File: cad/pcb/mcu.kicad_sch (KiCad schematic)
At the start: 22 parts, among them SW1 nRST, U1 nRF52810-QFxx, X1 SWD_Conn, Y1 32Meg, Y2 32.768k

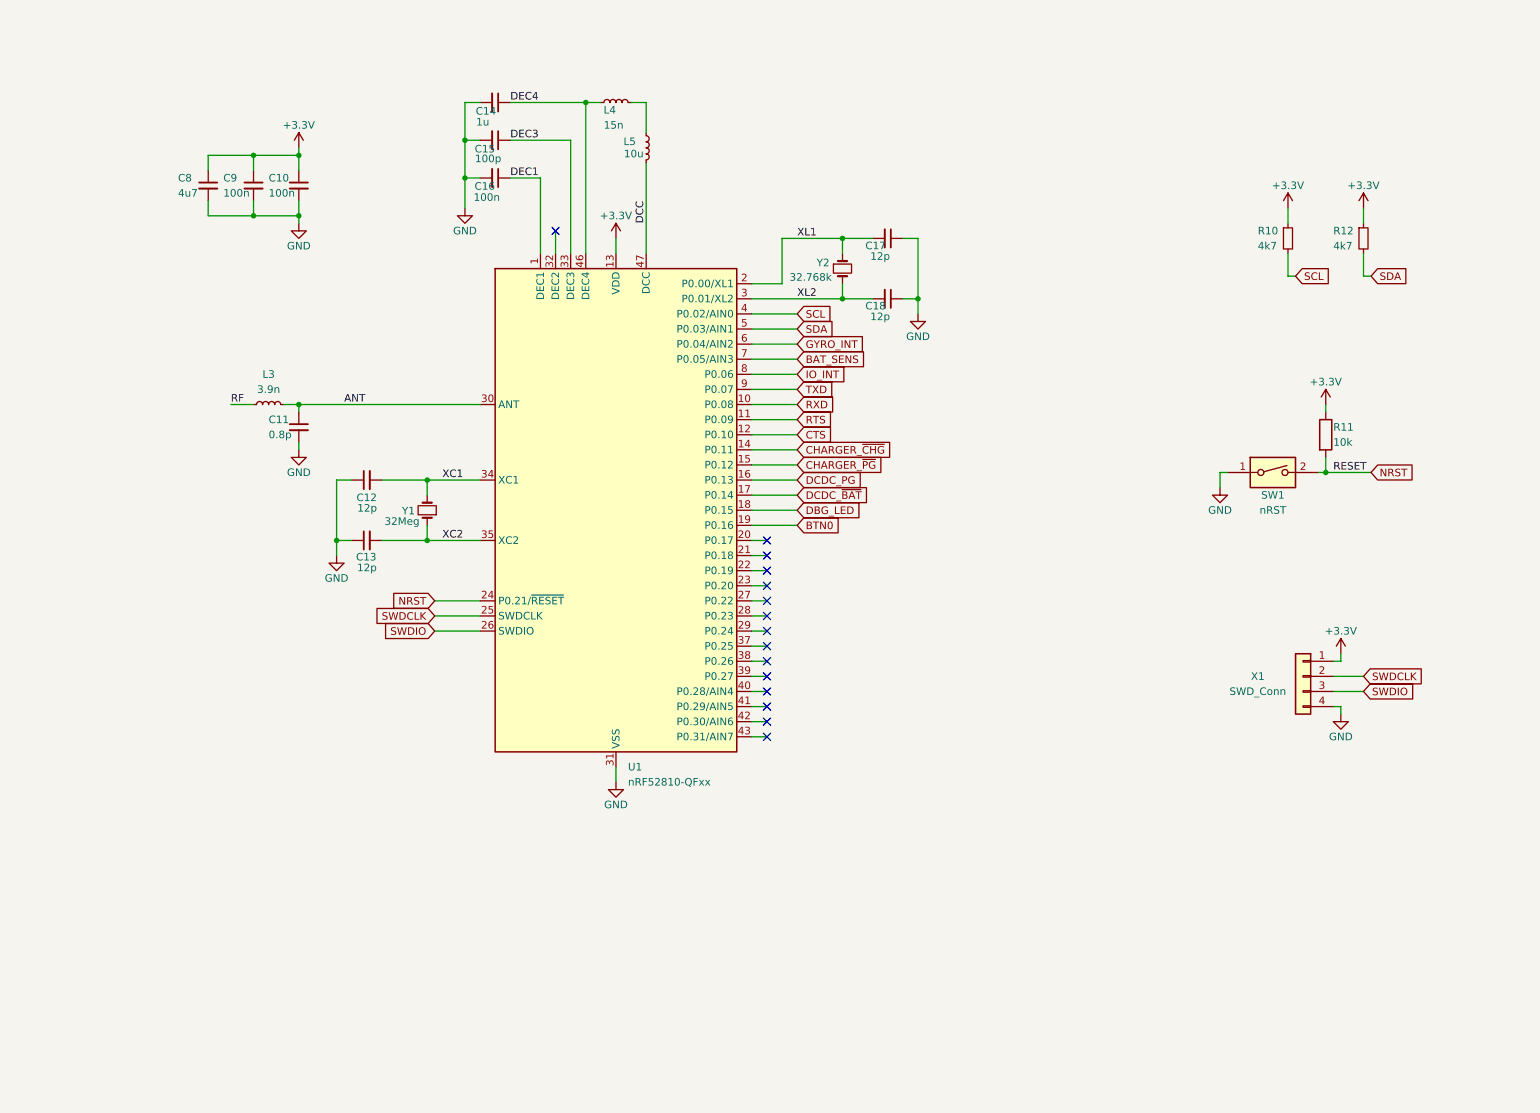
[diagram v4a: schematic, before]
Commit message: add LEDs for LED ring
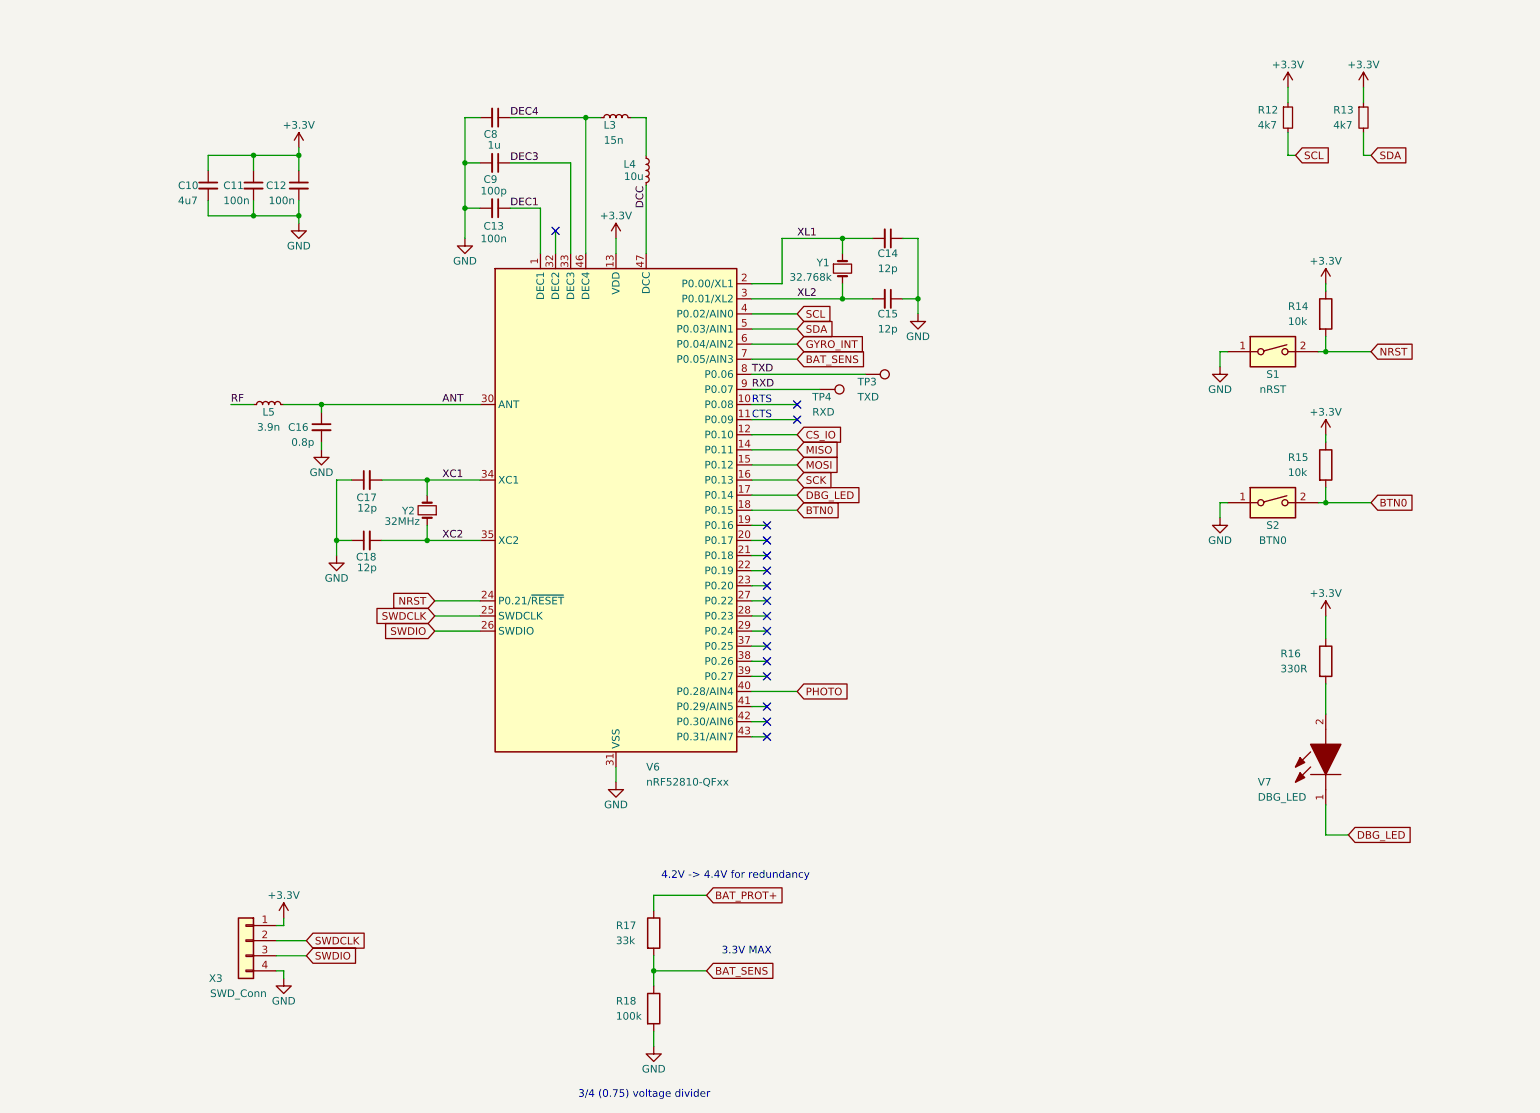
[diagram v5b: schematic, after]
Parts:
- added R15: 10k, symbol Device:R
- added R16: 330R, symbol Device:R
- added R17: 33k, symbol Device:R
- added R18: 100k, symbol Device:R
- added S2: BTN0, symbol Switch:SW_DIP_x01
- added TP3: TXD, symbol Connector:TestPoint
- added TP4: RXD, symbol Connector:TestPoint
- added V7: DBG_LED, LED red:LEDC1608X80N, symbol LED red:150060SS75000
- Y2: renamed from Y1; value 32Meg -> 32MHz
- renumbered C8 to C10, C9 to C11, C10 to C12, C16 to C13, C17 to C14, C18 to C15, C11 to C16, C12 to C17, C13 to C18, C14 to C8, C15 to C9, L4 to L3, L5 to L4, L3 to L5, R10 to R12, R12 to R13, R11 to R14, SW1 to S1, U1 to V6, X1 to X3, Y2 to Y1
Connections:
- net DCDC_~{BAT} is gone; now on net DBG_LED: V6.17 (P0.14)
- net IO_INT is gone; now on net TXD: V6.8 (P0.06)
- net BAT_SENS: now also R17.2, R18.1
- net BTN0: now also V6.18 (P0.15), R15.2, S2.2; no longer V6.19 (P0.16)
- net DBG_LED: now also V7.1; no longer V6.18 (P0.15)
- net GND: now also R18.2, S2.1
- net RXD: now also V6.9 (P0.07), TP4.1; no longer V6.10 (P0.08)
- net TXD: now also TP3.1; no longer V6.9 (P0.07)
- net PHOTO: now reaches V6.40 (P0.28/AIN4)
- net +3V3 renamed +3.3V
- net +3.3V: now also R15.1, R16.1
- net CHARGER_~{CHG} renamed MISO
- net CHARGER_~{PG} renamed MOSI
- net CTS renamed CS_IO
- net DCDC_PG renamed SCK
- net RTS: no longer names the net of V6.11 (P0.09)
- new net: R16.2, V7.2
- new net BAT_PROT+: R17.1
- no-connect marks 15 -> 17
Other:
- note added: "3.3V MAX"
- note added: "3/4 (0.75) voltage divider"
- note added: "4.2V -> 4.4V for redundancy"
- note added: "CTS"
- note added: "RTS"
- moved on the sheet: C13, C16, C8, C9, L3, L4, R12, R13, R14, S1, X3

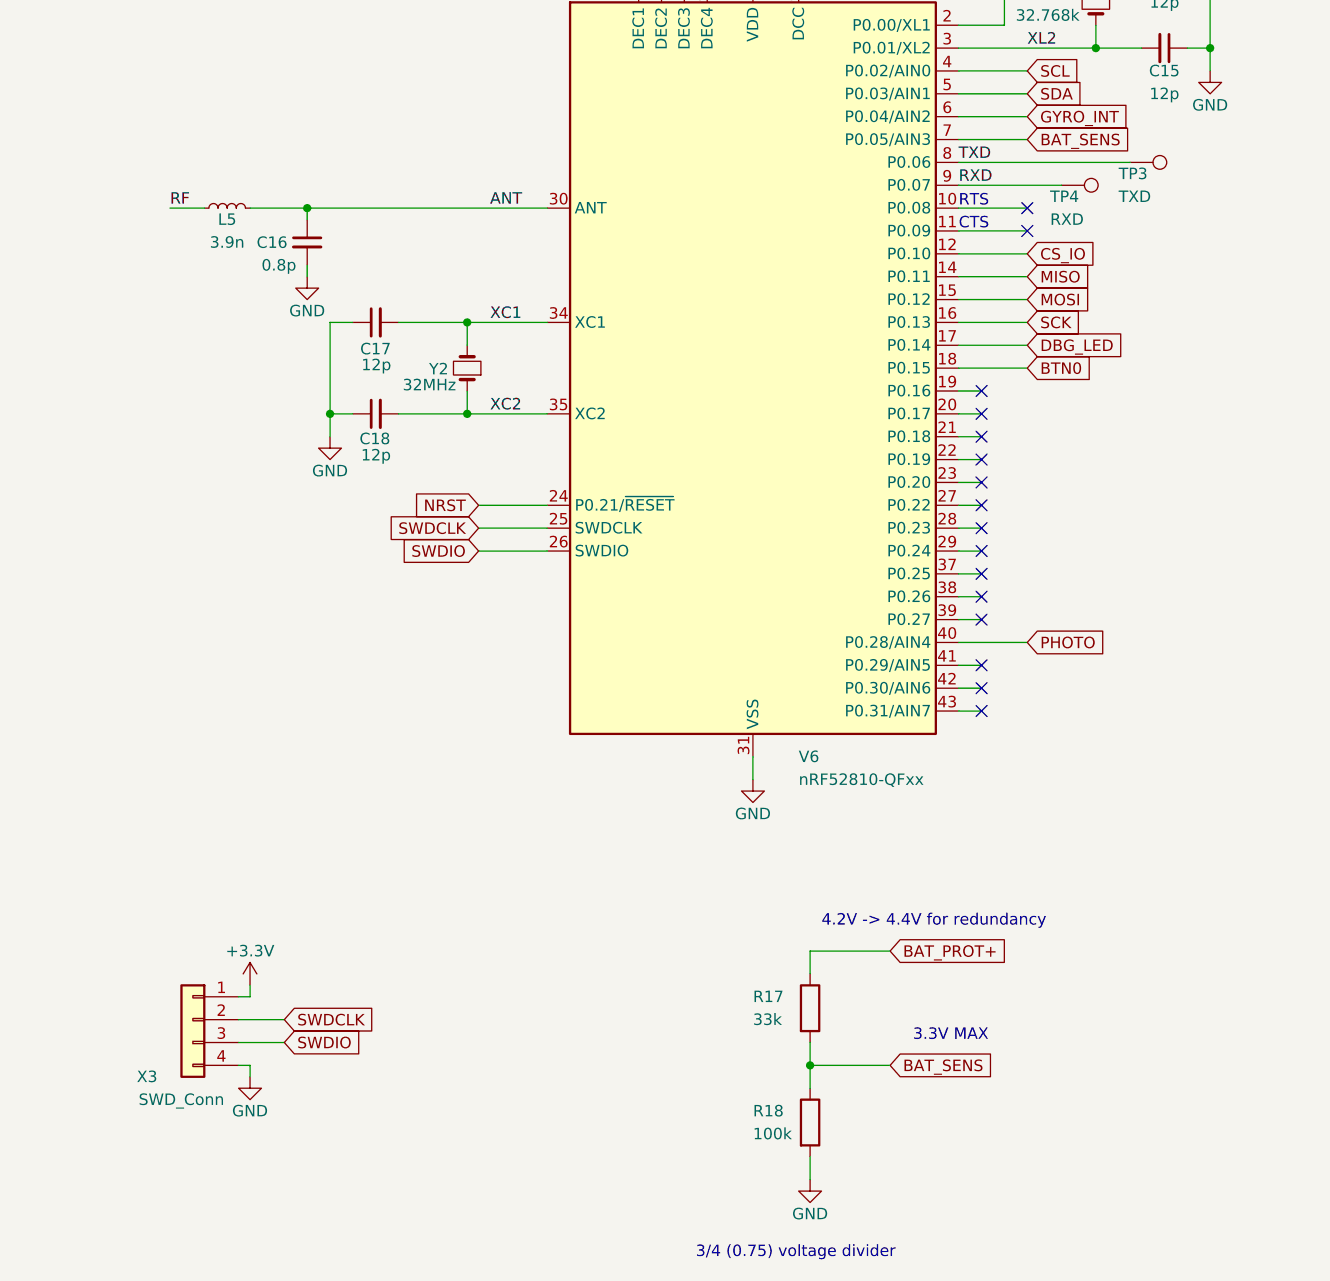
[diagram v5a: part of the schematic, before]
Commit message: add testpoints & connectors
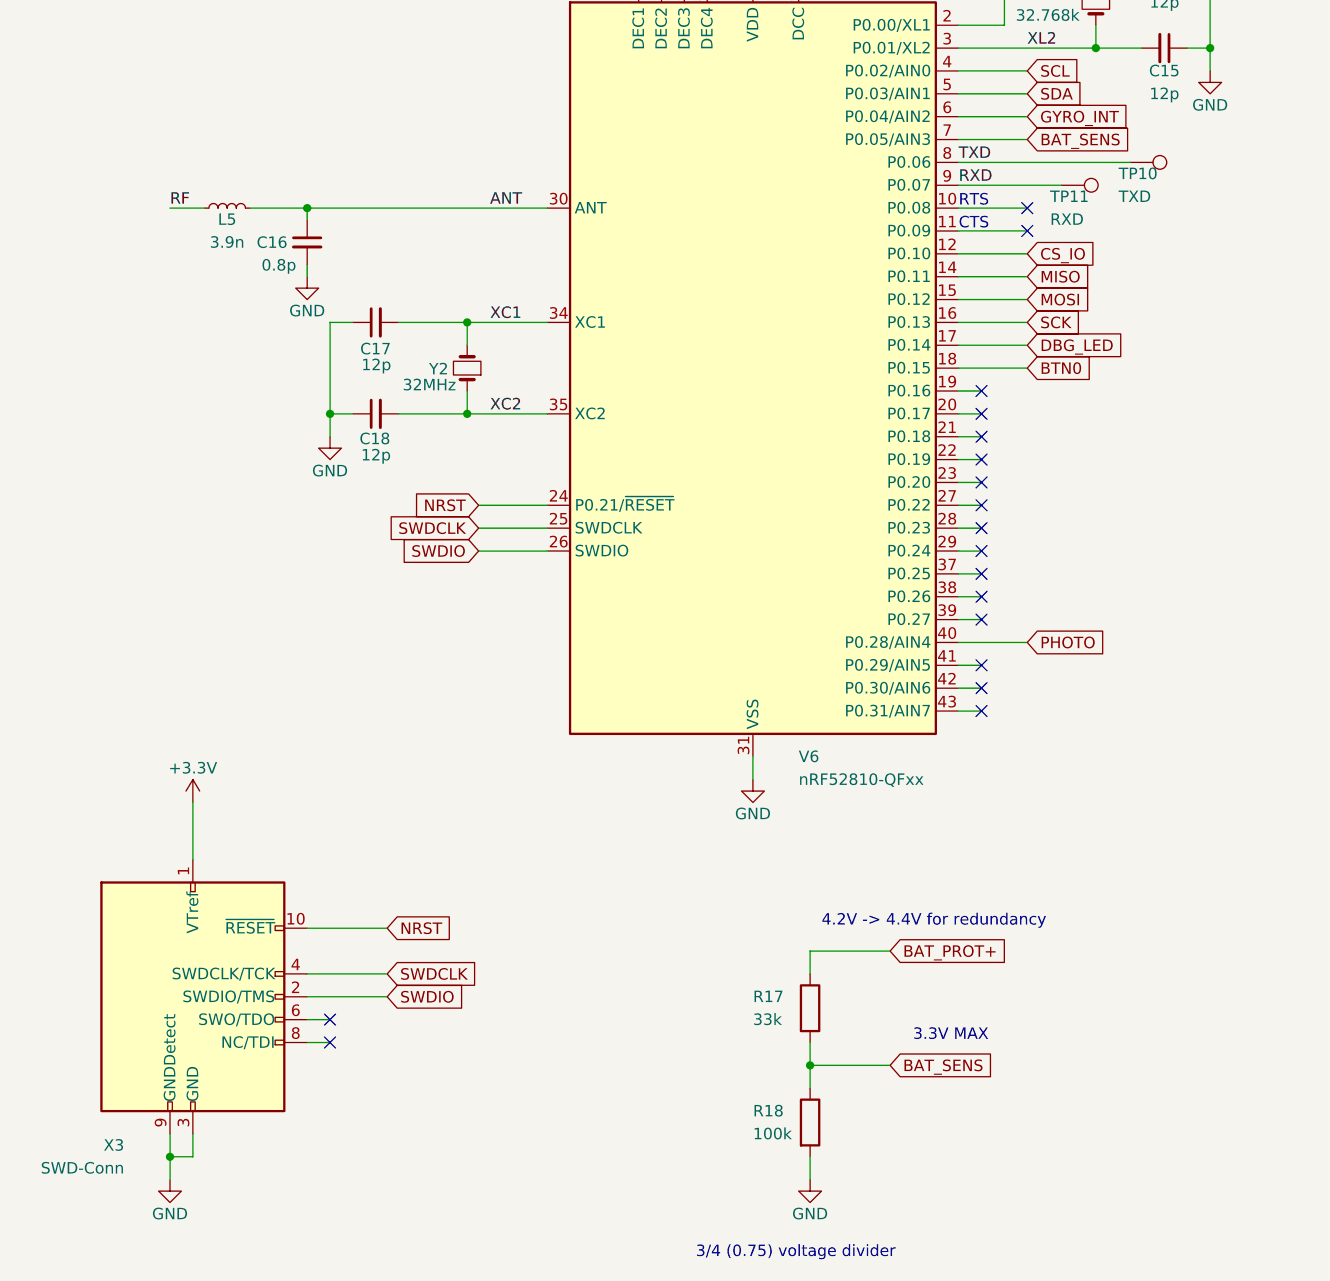
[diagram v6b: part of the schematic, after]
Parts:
- removed X3: SWD_Conn, symbol Connector_Generic:Conn_01x04
- added X3: SWD-Conn, Connector_PinHeader_1.27mm:PinHeader_2x05_P1.27mm_Vertical_SMD, symbol Connector:Conn_ARM_JTAG_SWD_10
- renumbered TP3 to TP10, TP4 to TP11
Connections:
- net +3.3V: now also X3.1 (VTref)
- net GND: now also X3.3 (GND), X3.5 (GND), X3.9 (GNDDetect)
- net NRST: now also X3.10 (~{RESET})
- net SWDCLK: now also X3.4 (SWDCLK/TCK)
- net SWDIO: now also X3.2 (SWDIO/TMS)
- no-connect marks 17 -> 19
